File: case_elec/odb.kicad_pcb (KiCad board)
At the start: 2 copper layers, 2 parts, among them U1 MPL3115A2, U2 Teensy3.5

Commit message: Mise à jour du pcb
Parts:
- removed U1: MPL3115A2, Package_LGA:NXP_LGA-8_3x5mm_P1.25mm_H1.1mm
- added REF**: BNO055, Adafruit_sensors:BNO055, F.Cu at (109.2, 53.3)
- added REF**: MPL3115A2, Adafruit_sensors:MPL3115A2, F.Cu at (134.2, 62.5)
- added REF**: Molex_Nano-Fit_105310-xx14_2x07_P2.50mm_Vertical, Connector_Molex:Molex_Nano-Fit_105310-xx14_2x07_P2.50mm_Vertical, F.Cu at (195.6, 76.4)
- added REF**: RYLR896, Reyax:RYLR896, F.Cu at (180.3, 50.8)
- added REF**: Ultimate_GPS, Adafruit_sensors:Ultimate_GPS, F.Cu at (116.8, 83.8)
- moved U2 21.0 mm to (154.9, 73.7), turned to -90 degrees
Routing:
- added copper zone on B.Cu, net (none)
- added copper zone on F.Cu, net (none)
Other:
- board outline added: 34.3 x 25.4 mm

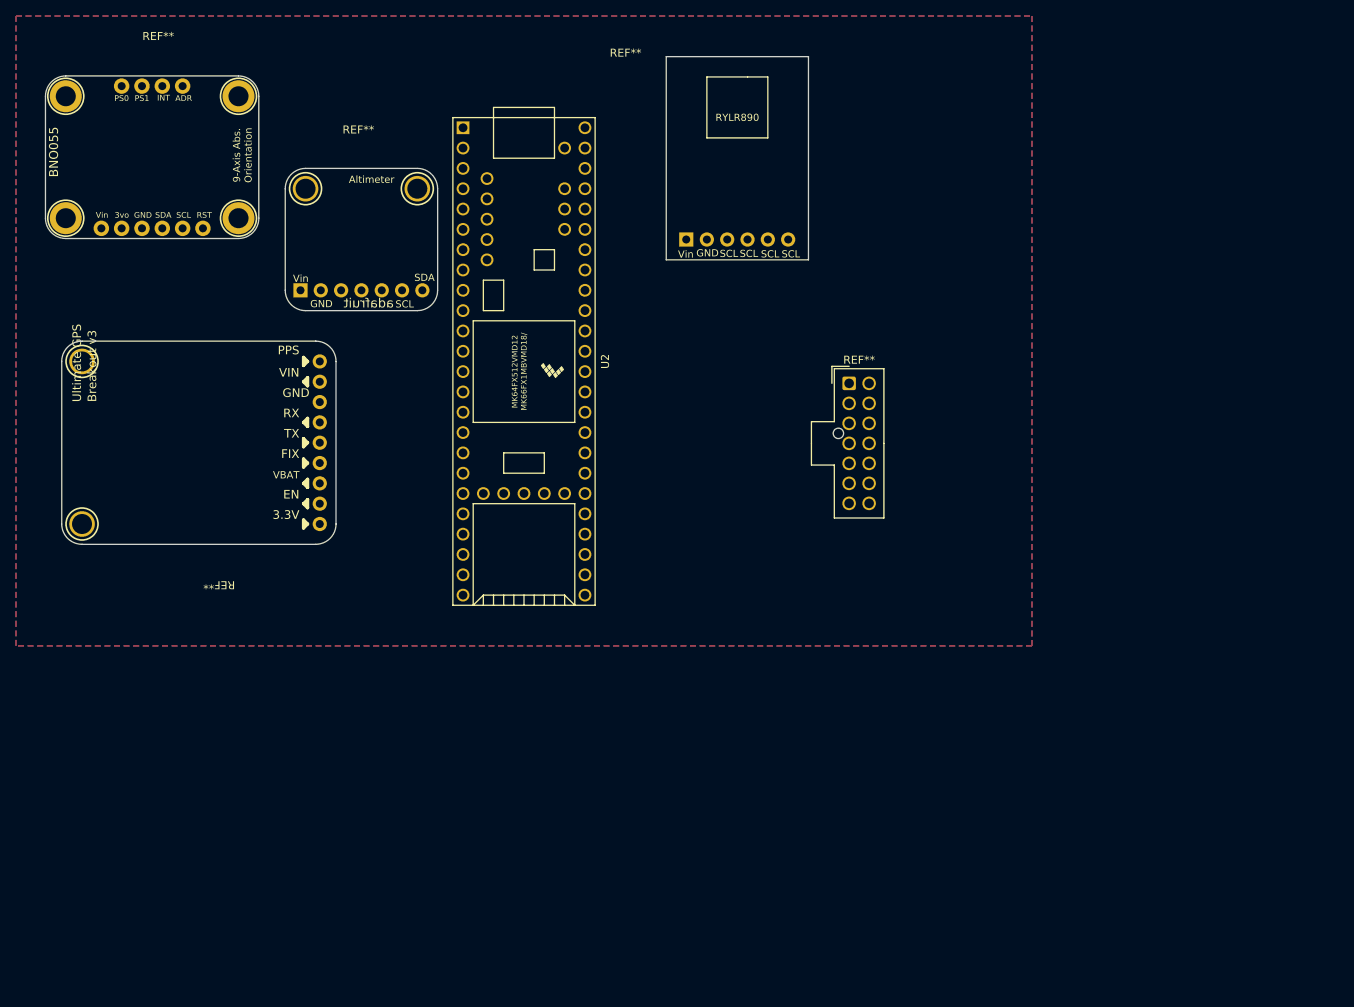
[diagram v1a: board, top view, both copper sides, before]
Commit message: agencement approximatif des composants du pcb
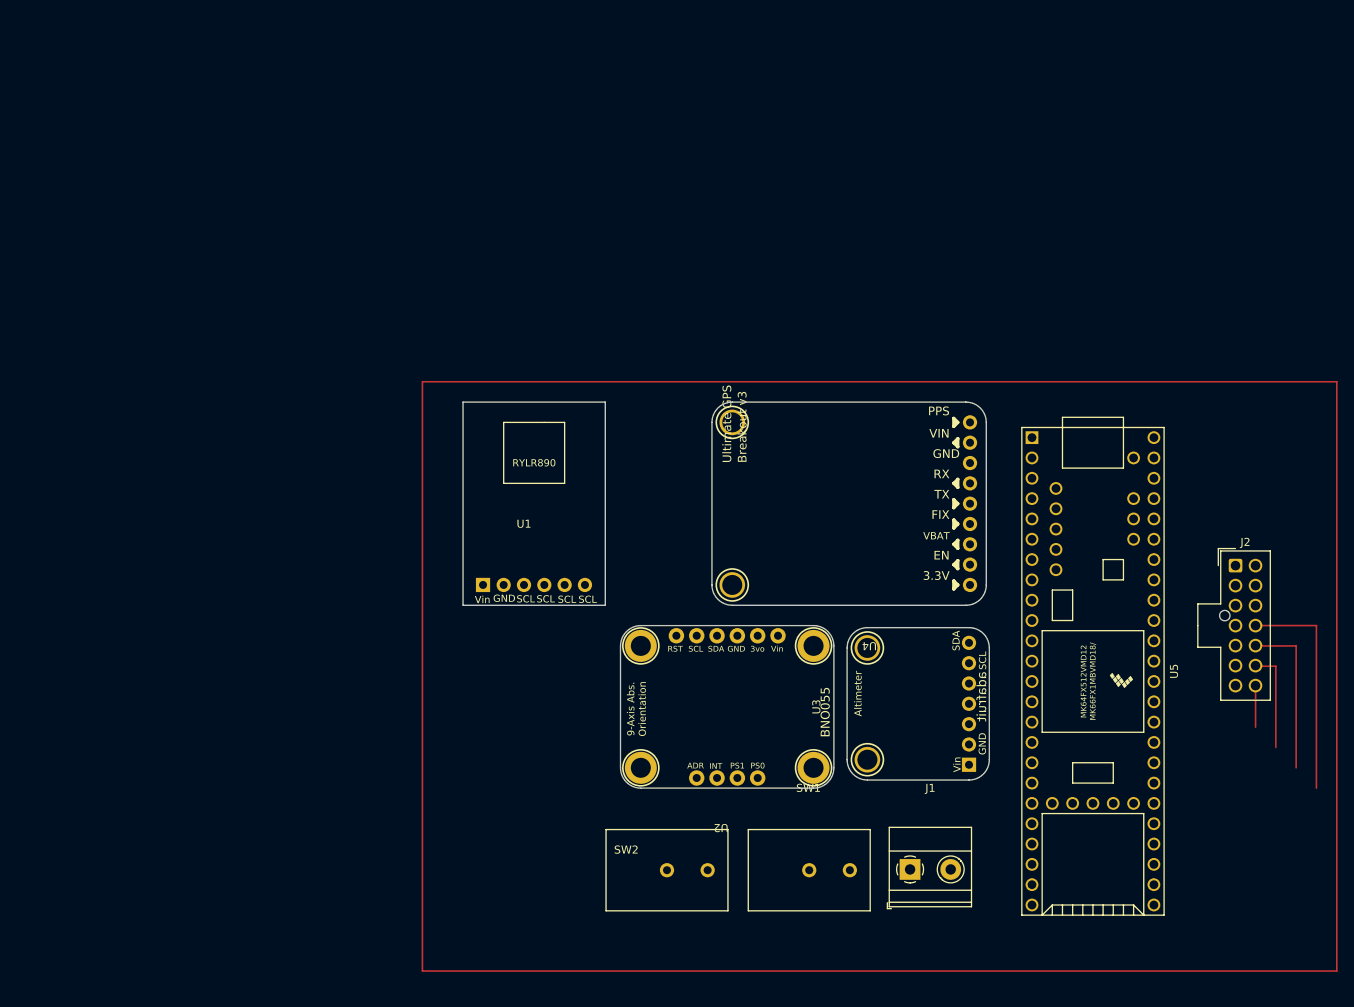
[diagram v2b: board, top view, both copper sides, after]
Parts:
- removed REF**: BNO055, Adafruit_sensors:BNO055
- removed REF**: MPL3115A2, Adafruit_sensors:MPL3115A2
- removed REF**: Molex_Nano-Fit_105310-xx14_2x07_P2.50mm_Vertical, Connector_Molex:Molex_Nano-Fit_105310-xx14_2x07_P2.50mm_Vertical
- removed REF**: RYLR896, Reyax:RYLR896
- removed REF**: Ultimate_GPS, Adafruit_sensors:Ultimate_GPS
- added J1: Screw_Terminal_01x02, TerminalBlock_Phoenix:TerminalBlock_Phoenix_MKDS-1,5-2-5.08_1x02_P5.08mm_Horizontal, F.Cu at (203.2, 137.2)
- added J2: Conn_02x07_Top_Bottom, Connector_Molex:Molex_Nano-Fit_105310-xx14_2x07_P2.50mm_Vertical, F.Cu at (243.9, 99.2)
- added SW1: SW_SPST, common_misc:SW, F.Cu at (183.0, 132.2)
- added SW2: SW_SPST, common_misc:SW, F.Cu at (165.2, 132.2)
- added U1: REYAX RYLR896, reyax:RYLR896, F.Cu at (154.9, 94.0)
- added U3: MPL3115A, Adafruit_sensors:MPL3115A2, F.Cu at (208.3, 116.8)
- added U4: Ultimate_GPS, Adafruit_sensors:Ultimate_GPS, F.Cu at (198.1, 91.4)
- added U5: Teensy3.5, teensy:Teensy35_36, F.Cu at (218.4, 113.7)
- U2: value Teensy3.5 -> BNO055; footprint teensy:Teensy35_36 -> Adafruit_sensors:BNO055
- moved U2 45.3 mm to (179.6, 111.6), turned to 180 degrees
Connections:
- U2 pad 1: unconnected-(U2-Pad1) -> +5V
- U2 pad 3: unconnected-(U2-Pad3) -> GND
- U2 pad 4: unconnected-(U2-Pad4) -> Net-(U2-Pad4)
- U2 pad 5: unconnected-(U2-Pad5) -> Net-(U2-Pad5)
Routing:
- removed copper zone on B.Cu, net (none)
- removed copper zone on F.Cu, net (none)

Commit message: pcb en cours de tracé
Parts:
- J1, J2, SW1, SW2, U1, U2, U3, U4, U5: moved to B.Cu
- moved J2 86.0 mm to (157.9, 99.1), turned to 180 degrees
- moved U2 42.9 mm to (222.2, 116.7), turned to 0 degrees
- moved U1 40.7 mm to (152.4, 134.6), turned to 180 degrees
- moved SW1 38.0 mm to (220.9, 134.7), turned to 180 degrees
- moved SW2 38.0 mm to (203.1, 134.7), turned to 180 degrees
- moved U5 33.9 mm to (184.6, 114.3)
- moved J1 28.1 mm to (231.1, 139.7), turned to 180 degrees
- moved U3 14.8 mm to (193.5, 117.2)
- moved U4 5.50 mm to (203.6, 91.4), turned to 0 degrees
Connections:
- U3 pad 7: Net-(U2-Pad5) -> Net-(U2-Pad4)
- U5 pad 10: Net-(U2-Pad5) -> Net-(U2-Pad4)
- U5 pad 9: Net-(U2-Pad4) -> Net-(U2-Pad5)
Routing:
- net +5V: track 0.00 -> 98.1 mm
- net Net-(SW2-Pad1): track 0.00 -> 40.0 mm
- net Net-(U1-Pad4): track 0.00 -> 36.8 mm
- net Net-(U1-Pad3): track 0.00 -> 33.3 mm
- net /A19: track 0.00 -> 32.8 mm
- net /A20: track 0.00 -> 28.2 mm
- net Net-(J1-Pad1): track 0.00 -> 27.0 mm
- net /A9: track 0.00 -> 26.9 mm
- net /A21: track 0.00 -> 23.7 mm
- net /A8: track 0.00 -> 21.4 mm
- net /A22: track 0.00 -> 17.2 mm
- net /A7: track 0.00 -> 15.0 mm
- net /A0: track 0.00 -> 11.6 mm
- net /A1: track 0.00 -> 11.6 mm
- net /A2: track 0.00 -> 11.6 mm
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- added copper zone on F.Cu, net GND
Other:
- board outline removed

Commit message: Ajout du plan de masse + intercom
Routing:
- net /A19: track 32.8 -> 44.0 mm
- net /A20: track 28.2 -> 36.9 mm
- net /A21: track 23.7 -> 29.7 mm
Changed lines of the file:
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@@
     )
   )
-  (gr_rect (start 124.46 77.47) (end 238.76 151.13) (layer "F.Cu") (width 0.2) (fill none))
+  (gr_rect (start 137.16 77.47) (end 238.76 151.13) (layer "F.Cu") (width 0.2) (fill none))
   (segment (start 231.14 139.7) (end 231.14 142.24) (width 0.4) (layer "F.Cu") (net 1))
   (segment (start 226.06 147.32) (end 218.44 147.32) (width 0.4) (layer "F.Cu") (net 1))
@@
   (segment (start 153.509063 95.410937) (end 157.450058 91.469942) (width 0.4) (layer "F.Cu") (net 12))
   (segment (start 153.509063 102.250969) (end 153.509063 95.410937) (width 0.4) (layer "F.Cu") (net 12))
-  (segment (start 155.358094 106.6) (end 152.909543 109.048551) (width 0.4) (layer "F.Cu") (net 13))
-  (segment (start 152.909543 109.048551) (end 152.909543 116.505243) (width 0.4) (layer "F.Cu") (net 13))
-  (segment (start 165.974242 129.569942) (end 169.347067 129.569942) (width 0.4) (layer "F.Cu") (net 13))
-  (segment (start 152.909543 116.505243) (end 165.974242 129.569942) (width 0.4) (layer "F.Cu") (net 13))
-  (segment (start 164.282092 127.029942) (end 169.347067 127.029942) (width 0.4) (layer "F.Cu") (net 14))
-  (segment (start 153.509063 110.949031) (end 153.509063 116.256913) (width 0.4) (layer "F.Cu") (net 14))
-  (segment (start 155.358094 109.1) (end 153.509063 110.949031) (width 0.4) (layer "F.Cu") (net 14))
-  (segment (start 153.509063 116.256913) (end 164.282092 127.029942) (width 0.4) (layer "F.Cu") (net 14))
-  (segment (start 154.108583 112.849511) (end 154.108583 116.008583) (width 0.4) (layer "F.Cu") (net 15))
-  (segment (start 155.358094 111.6) (end 154.108583 112.849511) (width 0.4) (layer "F.Cu") (net 15))
-  (segment (start 162.589942 124.489942) (end 169.347067 124.489942) (width 0.4) (layer "F.Cu") (net 15))
-  (segment (start 154.108583 116.008583) (end 162.589942 124.489942) (width 0.4) (layer "F.Cu") (net 15))
+  (segment (start 157.509942 129.569942) (end 169.347067 129.569942) (width 0.4) (layer "F.Cu") (net 13))
+  (segment (start 155.358094 106.6) (end 152.48 106.6) (width 0.4) (layer "F.Cu") (net 13))
+  (segment (start 147.32 111.76) (end 147.32 119.38) (width 0.4) (layer "F.Cu") (net 13))
+  (segment (start 147.32 119.38) (end 157.509942 129.569942) (width 0.4) (layer "F.Cu") (net 13))
+  (segment (start 152.48 106.6) (end 147.32 111.76) (width 0.4) (layer "F.Cu") (net 13))
+  (segment (start 152.52 109.1) (end 155.358094 109.1) (width 0.4) (layer "F.Cu") (net 14))
+  (segment (start 169.347067 127.029942) (end 157.509942 127.029942) (width 0.4) (layer "F.Cu") (net 14))
+  (segment (start 149.86 111.76) (end 152.52 109.1) (width 0.4) (layer "F.Cu") (net 14))
+  (segment (start 157.509942 127.029942) (end 149.86 119.38) (width 0.4) (layer "F.Cu") (net 14))
+  (segment (start 149.86 119.38) (end 149.86 111.76) (width 0.4) (layer "F.Cu") (net 14))
+  (segment (start 152.56 111.6) (end 152.4 111.76) (width 0.4) (layer "F.Cu") (net 15))
+  (segment (start 155.358094 111.6) (end 152.56 111.6) (width 0.4) (layer "F.Cu") (net 15))
+  (segment (start 152.4 111.76) (end 152.4 119.38) (width 0.4) (layer "F.Cu") (net 15))
+  (segment (start 157.509942 124.489942) (end 169.347067 124.489942) (width 0.4) (layer "F.Cu") (net 15))
+  (segment (start 152.4 119.38) (end 157.509942 124.489942) (width 0.4) (layer "F.Cu") (net 15))
   (segment (start 163.208036 121.949942) (end 169.347067 121.949942) (width 0.4) (layer "F.Cu") (net 16))
   (segment (start 155.358094 114.1) (end 163.208036 121.949942) (width 0.4) (layer "F.Cu") (net 16))
@@
   (zone (net 2) (net_name "GND") (layer "F.Cu") (name "plan de masse") (hatch edge 0.508)
     (connect_pads (clearance 0.508))
-    (min_thickness 0.254)
-    (fill (thermal_gap 0.508) (thermal_bridge_width 0.508))
+    (min_thickness 0.254) (filled_areas_thickness no)
+    (fill yes (thermal_gap 0.508) (thermal_bridge_width 0.508))
     (polygon
       (pts
-        (xy 241.3 147.32)
-        (xy 142.24 147.32)
-        (xy 142.24 78.74)
-        (xy 241.3 78.74)
+        (xy 236.22 149.86)
+        (xy 139.7 149.86)
+        (xy 139.7 78.74)
+        (xy 236.22 78.74)
       )
     )

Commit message: Jade's participation
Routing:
- net +5V: track 98.1 -> 203.3 mm
- net Net-(U2-Pad5): track 0.00 -> 44.3 mm
- net Net-(U2-Pad4): track 7.62 -> 41.9 mm
- net Net-(U1-Pad3): track 33.3 -> 39.0 mm
- net Net-(U1-Pad4): track 36.8 -> 42.1 mm
- net Net-(SW2-Pad1): track 40.0 -> 45.3 mm
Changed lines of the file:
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@@
   (segment (start 163.208036 121.949942) (end 169.347067 121.949942) (width 0.4) (layer "F.Cu") (net 16))
   (segment (start 155.358094 114.1) (end 163.208036 121.949942) (width 0.4) (layer "F.Cu") (net 16))
-  (segment (start 169.347067 83.849942) (end 170.687556 85.190431) (width 0.4) (layer "F.Cu") (net 17))
-  (segment (start 184.090212 97.749453) (end 189.815641 97.749453) (width 0.4) (layer "F.Cu") (net 17))
+  (segment (start 169.347067 83.849942) (end 174.457009 78.74) (width 0.25) (layer "F.Cu") (net 17))
   (segment (start 206.896489 138.506489) (end 208.185 139.795) (width 0.4) (layer "F.Cu") (net 17))
-  (segment (start 187.321547 120.609453) (end 184.090212 120.609453) (width 0.4) (layer "F.Cu") (net 17))
-  (segment (start 189.815641 97.749453) (end 191.045094 96.52) (width 0.4) (layer "F.Cu") (net 17))
-  (segment (start 182.860759 96.52) (end 184.090212 97.749453) (width 0.4) (layer "F.Cu") (net 17))
-  (segment (start 170.687556 88.574065) (end 178.633491 96.52) (width 0.4) (layer "F.Cu") (net 17))
-  (segment (start 184.090212 120.609453) (end 178.633491 115.152732) (width 0.4) (layer "F.Cu") (net 17))
-  (segment (start 178.633491 115.152732) (end 178.633491 96.52) (width 0.4) (layer "F.Cu") (net 17))
-  (segment (start 170.687556 85.190431) (end 170.687556 88.574065) (width 0.4) (layer "F.Cu") (net 17))
+  (segment (start 198.12 96.52) (end 210.82 83.82) (width 0.25) (layer "F.Cu") (net 17))
+  (segment (start 236.22 119.38) (end 221.398094 119.38) (width 0.25) (layer "F.Cu") (net 17))
+  (segment (start 236.22 109.22) (end 236.22 119.38) (width 0.25) (layer "F.Cu") (net 17))
+  (segment (start 221.398094 119.38) (end 215.048094 113.03) (width 0.25) (layer "F.Cu") (net 17))
   (segment (start 191.172094 137.985072) (end 191.172094 124.46) (width 0.4) (layer "F.Cu") (net 17))
+  (segment (start 205.74 78.74) (end 236.22 109.22) (width 0.25) (layer "F.Cu") (net 17))
   (segment (start 191.693511 138.506489) (end 206.896489 138.506489) (width 0.4) (layer "F.Cu") (net 17))
-  (segment (start 178.633491 96.52) (end 182.860759 96.52) (width 0.4) (layer "F.Cu") (net 17))
   (segment (start 191.693511 138.506489) (end 191.172094 137.985072) (width 0.4) (layer "F.Cu") (net 17))
-  (segment (start 191.172094 124.46) (end 187.321547 120.609453) (width 0.4) (layer "F.Cu") (net 17))
+  (segment (start 174.457009 78.74) (end 205.74 78.74) (width 0.25) (layer "F.Cu") (net 17))
+  (segment (start 215.048094 113.03) (end 215.048094 132.931906) (width 0.25) (layer "F.Cu") (net 17))
+  (segment (start 191.045094 96.52) (end 198.12 96.52) (width 0.25) (layer "F.Cu") (net 17))
+  (segment (start 215.048094 132.931906) (end 208.185 139.795) (width 0.25) (layer "F.Cu") (net 17))
   (segment (start 190.405 139.795) (end 191.693511 138.506489) (width 0.4) (layer "F.Cu") (net 17))
-  (segment (start 191.810547 143.469453) (end 195.485 139.795) (width 0.4) (layer "F.Cu") (net 18))
-  (segment (start 157.52 142.24) (end 158.749453 143.469453) (width 0.4) (layer "F.Cu") (net 18))
-  (segment (start 158.749453 143.469453) (end 191.810547 143.469453) (width 0.4) (layer "F.Cu") (net 18))
-  (segment (start 153.688511 140.951489) (end 183.268614 140.951489) (width 0.4) (layer "F.Cu") (net 20))
-  (segment (start 183.268614 140.951489) (end 184.587067 142.269942) (width 0.4) (layer "F.Cu") (net 20))
-  (segment (start 152.4 142.24) (end 153.688511 140.951489) (width 0.4) (layer "F.Cu") (net 20))
-  (segment (start 153.569569 138.530431) (end 183.387556 138.530431) (width 0.4) (layer "F.Cu") (net 21))
-  (segment (start 149.86 142.24) (end 153.569569 138.530431) (width 0.4) (layer "F.Cu") (net 21))
-  (segment (start 183.387556 138.530431) (end 184.587067 139.729942) (width 0.4) (layer "F.Cu") (net 21))
+  (segment (start 165.14 149.86) (end 185.42 149.86) (width 0.4) (layer "F.Cu") (net 18))
+  (segment (start 185.42 149.86) (end 195.485 139.795) (width 0.4) (layer "F.Cu") (net 18))
+  (segment (start 157.52 142.24) (end 165.14 149.86) (width 0.4) (layer "F.Cu") (net 18))
+  (segment (start 167.64 147.32) (end 180.34 147.32) (width 0.4) (layer "F.Cu") (net 20))
+  (segment (start 154.94 139.7) (end 160.02 139.7) (width 0.4) (layer "F.Cu") (net 20))
+  (segment (start 160.02 139.7) (end 167.64 147.32) (width 0.4) (layer "F.Cu") (net 20))
+  (segment (start 184.587067 143.072933) (end 184.587067 142.269942) (width 0.4) (layer "F.Cu") (net 20))
+  (segment (start 180.34 147.32) (end 184.587067 143.072933) (width 0.4) (layer "F.Cu") (net 20))
+  (segment (start 152.4 142.24) (end 154.94 139.7) (width 0.4) (layer "F.Cu") (net 20))
+  (segment (start 160.039256 137.16) (end 167.659256 144.78) (width 0.4) (layer "F.Cu") (net 21))
+  (segment (start 167.659256 144.78) (end 179.537009 144.78) (width 0.4) (layer "F.Cu") (net 21))
+  (segment (start 149.86 142.24) (end 154.94 137.16) (width 0.4) (layer "F.Cu") (net 21))
+  (segment (start 154.94 137.16) (end 160.039256 137.16) (width 0.4) (layer "F.Cu") (net 21))
+  (segment (start 179.537009 144.78) (end 184.587067 139.729942) (width 0.4) (layer "F.Cu") (net 21))
   (segment (start 188.662036 106.709942) (end 191.172094 109.22) (width 0.4) (layer "F.Cu") (net 24))
+  (segment (start 192.678114 107.71398) (end 191.172094 109.22) (width 0.25) (layer "F.Cu") (net 24))
+  (segment (start 222.668094 113.03) (end 217.352074 107.71398) (width 0.25) (layer "F.Cu") (net 24))
   (segment (start 184.587067 106.709942) (end 188.662036 106.709942) (width 0.4) (layer "F.Cu") (net 24))
+  (segment (start 217.352074 107.71398) (end 192.678114 107.71398) (width 0.25) (layer "F.Cu") (net 24))
+  (segment (start 216.348036 104.169942) (end 225.208094 113.03) (width 0.25) (layer "F.Cu") (net 25))
+  (segment (start 184.587067 104.169942) (end 216.348036 104.169942) (width 0.25) (layer "F.Cu") (net 25))
   (segment (start 187.097125 88.9) (end 184.587067 86.389942) (width 0.4) (layer "F.Cu") (net 34))
   (segment (start 191.045094 88.9) (end 187.097125 88.9) (width 0.4) (layer "F.Cu") (net 34))
@@
     (polygon
       (pts
-        (xy 236.22 149.86)
-        (xy 139.7 149.86)
-        (xy 139.7 78.74)
-        (xy 236.22 78.74)
+        (xy 238.76 152.4)
+        (xy 137.16 152.4)
+        (xy 137.16 76.2)
+        (xy 238.76 76.2)
       )
     )

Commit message: complétion du pcb
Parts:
- added REF**: R_1206, Resistor_SMD:R_1206_3216Metric_Pad1.30x1.75mm_HandSolder, F.Cu at (148.2, 69.0)
- moved U1 45.5 mm to (111.9, 113.9)
- moved J2 45.5 mm to (117.3, 78.4)
- moved J1 45.5 mm to (190.6, 119.0)
- moved SW1 45.5 mm to (180.4, 114.0)
- moved SW2 45.5 mm to (162.6, 114.0)
- moved U2 45.5 mm to (181.6, 96.0)
- moved U5 45.5 mm to (144.1, 93.6)
- moved U3 43.7 mm to (152.7, 101.6)
- moved U4 42.7 mm to (165.0, 73.3)
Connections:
- U4 pad 4: Net-(U4-Pad4) -> unconnected-(U4-Pad4)
- U4 pad 6: GND -> Net-(U4-Pad6)
- U4 pad 7: +5V -> GND
- U4 pad 8: unconnected-(U4-Pad8) -> +5V
- U4 pad 9: (no net) -> unconnected-(U4-Pad9)
- U5 pad 2: Net-(U4-Pad4) -> Net-(U4-Pad5)
- U5 pad 3: Net-(U4-Pad5) -> Net-(U4-Pad6)
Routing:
- net /A9: track 26.9 -> 36.8 mm
- net Net-(U4-Pad6): track 0.00 -> 9.36 mm
- net /A8: track 21.4 -> 29.6 mm
- net Net-(U4-Pad4): track 7.50 -> 0.00 mm
- net +5V: track 203.3 -> 196.0 mm
- net Net-(U2-Pad4): track 41.9 -> 45.6 mm
- net Net-(U4-Pad5): track 7.50 -> 10.2 mm
- net Net-(J1-Pad1): track 27.0 -> 24.9 mm
- net Net-(SW2-Pad1): track 45.3 -> 44.2 mm

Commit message: ajout de zones keepout
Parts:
- moved J1 2.23 mm to (190.6, 121.2)
- moved SW1 2.23 mm to (180.4, 116.2)
- moved SW2 2.23 mm to (162.6, 116.2)
- moved U3 2.23 mm to (152.7, 103.8)
- moved U5 2.23 mm to (144.1, 95.9)
- moved J2 2.23 mm to (117.3, 80.6)
- moved REF** 2.23 mm to (148.2, 71.2)
- moved U1 2.23 mm to (111.9, 116.1)
- moved U2 2.23 mm to (181.6, 98.2)
- moved U4 2.23 mm to (165.0, 75.5)
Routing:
- net +5V: track 196.0 -> 193.0 mm
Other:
- board outline added: 98 x 79 mm
